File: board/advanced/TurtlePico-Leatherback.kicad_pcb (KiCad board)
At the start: 2 copper layers, 126 parts, among them J1 Micro_SD, J10 AudioJack3, J11 LED, J12 LED, J13 UltraSonic, J14 Debug, J15 Display, J16 TouchDisplay, J17 I/O Pins, J2 Jack-DC, J3 USB_C_Receptacle_USB2.0_16P, J4 RMotor, J5 LMotor, J6 FR_ESC, J7 FL_ESC, J8 RR_ESC, J9 RL_ESC, Q1 DMP6050SSD, Q2 2SC4213, Q3 2SC4213, SW1 SW_Bootsel, SW2 SW_Reset, SW3 SW_{R}, SW4 SW_{L}, SW5 SW_DIP_x04, U1 RP2350B-QFN80, U2 W25Q128JVS, U3 AP63203WU, U4 STUSB4500QTR, U5 DRV8835DSSR, U6 INA260, U7 BNO086, U8 BME280, U9 PCM5102A, Y1 ABM8-272-T3, Y2 ABS06-32.768KHZ-T

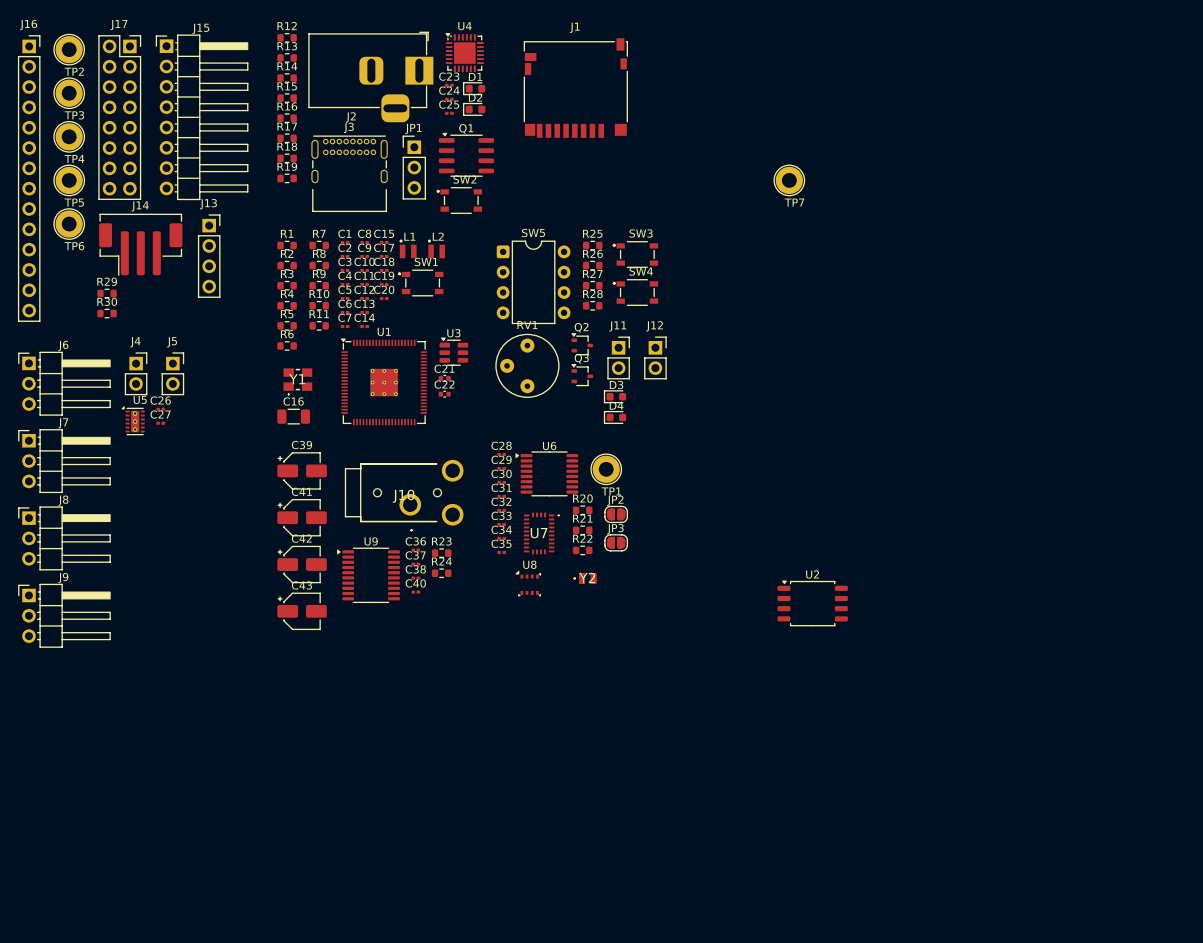
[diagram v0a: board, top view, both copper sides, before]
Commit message: put footprints and change schematics
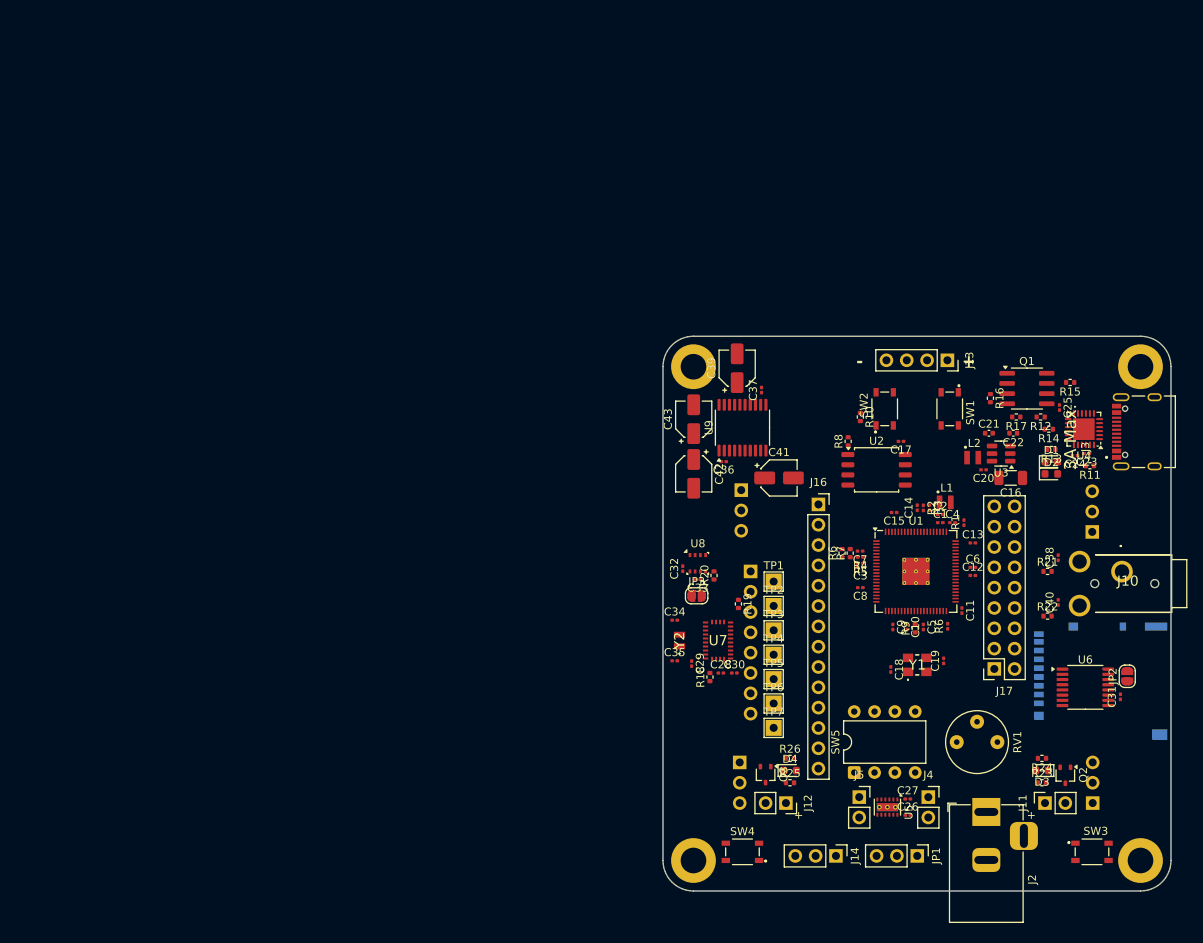
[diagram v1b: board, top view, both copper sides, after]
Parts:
- removed R29: 2k, Resistor_SMD:R_0603_1608Metric
- removed R30: 1k, Resistor_SMD:R_0603_1608Metric
- removed the R7 at (111.6, 66.1)
- removed the R8 at (111.6, 68.6)
- added G***: LOGO, PCBWay:PCBWay, B.Cu at (191.9, 90.8)
- added G***: LOGO, JinPro:JinPro, B.Cu at (178.7, 90.8)
- added R6: 4.7k, Resistor_SMD:R_0402_1005Metric, F.Cu at (176.9, 104.5)
- added REF**: MountingHole_3.2mm_M3_DIN965_Pad, MountingHole:MountingHole_3.2mm_M3_DIN965_Pad, F.Cu at (214.2, 142.9)
- added REF**: MountingHole_3.2mm_M3_DIN965_Pad, MountingHole:MountingHole_3.2mm_M3_DIN965_Pad, F.Cu at (158.3, 81.2)
- added REF**: MountingHole_3.2mm_M3_DIN965_Pad, MountingHole:MountingHole_3.2mm_M3_DIN965_Pad, F.Cu at (214.2, 81.2)
- added REF**: MountingHole_3.2mm_M3_DIN965_Pad, MountingHole:MountingHole_3.2mm_M3_DIN965_Pad, F.Cu at (158.3, 142.9)
- J1: footprint Connector_Card:microSD_HC_Hirose_DM3D-SF -> Connector_Card:microSD_HC_Hirose_DM3AT-SF-PEJM5; moved to B.Cu
- J11: value LED -> LED_{R}
- J12: value LED -> LED_{L}
- J14: footprint Connector_JST:JST_PH_B3B-PH-SM4-TB_1x03-1MP_P2.00mm_Vertical -> Connector_PinHeader_2.54mm:PinHeader_1x03_P2.54mm_Vertical
- J15, J6, J7, J8, J9: moved to B.Cu
- J17: value I/O Pins -> Conn_02x09_Odd_Even; footprint Connector_PinSocket_2.54mm:PinSocket_2x08_P2.54mm_Vertical -> Connector_PinSocket_2.54mm:PinSocket_2x09_P2.54mm_Vertical
- J3: footprint Connector_USB:USB_C_Receptacle_GCT_USB4085 -> NELTRON_5077CR-16SMC2-BK-TR:NELTRON_5077CR-16SMC2-BK-TR
- R1, R2, R3, R4, R5, R6: footprint Resistor_SMD:R_0603_1608Metric -> Resistor_SMD:R_0201_0603Metric
- R10: renamed from R12; footprint Resistor_SMD:R_0603_1608Metric -> Resistor_SMD:R_0402_1005Metric
- R11: renamed from R13; footprint Resistor_SMD:R_0603_1608Metric -> Resistor_SMD:R_0402_1005Metric
- R12: renamed from R14; footprint Resistor_SMD:R_0603_1608Metric -> Resistor_SMD:R_0402_1005Metric
- R13: renamed from R15; footprint Resistor_SMD:R_0603_1608Metric -> Resistor_SMD:R_0402_1005Metric
- R14: renamed from R16; footprint Resistor_SMD:R_0603_1608Metric -> Resistor_SMD:R_0402_1005Metric
- R15: renamed from R17; footprint Resistor_SMD:R_0603_1608Metric -> Resistor_SMD:R_0402_1005Metric
- R16: renamed from R18; footprint Resistor_SMD:R_0603_1608Metric -> Resistor_SMD:R_0402_1005Metric
- R17: renamed from R19; footprint Resistor_SMD:R_0603_1608Metric -> Resistor_SMD:R_0402_1005Metric
- R18: renamed from R20; footprint Resistor_SMD:R_0603_1608Metric -> Resistor_SMD:R_0402_1005Metric
- R19: renamed from R21; footprint Resistor_SMD:R_0603_1608Metric -> Resistor_SMD:R_0402_1005Metric
- R20: renamed from R22; footprint Resistor_SMD:R_0603_1608Metric -> Resistor_SMD:R_0402_1005Metric
- R21: renamed from R23; footprint Resistor_SMD:R_0603_1608Metric -> Resistor_SMD:R_0402_1005Metric
- R22: renamed from R24; footprint Resistor_SMD:R_0603_1608Metric -> Resistor_SMD:R_0402_1005Metric
- R23: renamed from R25; footprint Resistor_SMD:R_0603_1608Metric -> Resistor_SMD:R_0402_1005Metric
- R24: renamed from R26; footprint Resistor_SMD:R_0603_1608Metric -> Resistor_SMD:R_0402_1005Metric
- R25: renamed from R27; footprint Resistor_SMD:R_0603_1608Metric -> Resistor_SMD:R_0402_1005Metric
- R26: renamed from R28; footprint Resistor_SMD:R_0603_1608Metric -> Resistor_SMD:R_0402_1005Metric
- R7: renamed from R9; footprint Resistor_SMD:R_0603_1608Metric -> Resistor_SMD:R_0402_1005Metric
- R8: renamed from R10; footprint Resistor_SMD:R_0603_1608Metric -> Resistor_SMD:R_0402_1005Metric
- R9: renamed from R11; footprint Resistor_SMD:R_0603_1608Metric -> Resistor_SMD:R_0402_1005Metric
- TP1, TP2, TP3, TP4, TP5, TP6, TP7: footprint TestPoint:TestPoint_Loop_D2.50mm_Drill1.85mm -> TestPoint:TestPoint_THTPad_2.0x2.0mm_Drill1.0mm
- moved J8 137.7 mm to (208.2, 135.8)
- moved J6 134.6 mm to (208.2, 101.9)
- moved J17 133.2 mm to (195.9, 119.0), turned to 180 degrees
- moved J2 116.7 mm to (194.9, 136.9), turned to 90 degrees
- moved J14 115.3 mm to (176.1, 142.4), turned to -90 degrees
- moved J16 114.1 mm to (174.0, 98.4)
- moved J4 112.9 mm to (187.7, 135.0)
- moved R11 112.6 mm to (207.9, 93.6), turned to 180 degrees
- moved TP2 112.2 mm to (168.4, 111.1)
- moved TP3 110.7 mm to (168.4, 114.2)
- moved TP4 109.3 mm to (168.4, 117.2)
- moved JP1 108.6 mm to (186.3, 142.4), turned to -90 degrees
- moved TP5 107.9 mm to (168.4, 120.3)
- moved TP6 106.5 mm to (168.4, 123.3)
- moved J3 106.3 mm to (212.3, 89.4), turned to 90 degrees
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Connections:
- net TRIG renamed TRIG/UART_{RX}
- C40 pad 1: Net-(C38-Pad1) -> Net-(C40-Pad1)
- J10 pad R: Net-(C38-Pad1) -> Net-(C40-Pad1)
- J13 pad 3: Net-(J13-Pin_3) -> Echo/UART_{TX}
- J17 pad 10: I/O_{6} -> I/O_{8}
- J17 pad 11: I/O_{7} -> I/O_{9}
- J17 pad 12: I/O_{8} -> I/O_{10}
- J17 pad 13: I/O_{9} -> I/O_{11}
- J17 pad 14: I/O_{10} -> I/O_{12}
- J17 pad 15: I/O_{11} -> I/O_{13}
- J17 pad 16: I/O_{12} -> I/O_{14}
- J17 pad 8: GND -> I/O_{6}
- J17 pad 9: GND -> I/O_{7}
- Q1 pad 7: Net-(Q1A-D1-Pad7) -> VBUS
- Q1 pad 8: Net-(Q1A-D1-Pad7) -> VBUS
- R15 pad 2: Net-(Q1A-D1-Pad7) -> VBUS_{USB}
- R22 pad 2: Net-(C38-Pad1) -> Net-(C40-Pad1)
- U1 pad 40: Net-(U1-GPIO32) -> I/O_{0}
- U1 pad 42: Net-(U1-GPIO33) -> I/O_{1}
- U1 pad 43: I/O_{0} -> I/O_{2}
- U1 pad 44: I/O_{1} -> I/O_{3}
- U1 pad 45: I/O_{2} -> I/O_{4}
- U1 pad 46: I/O_{3} -> I/O_{5}
- U1 pad 47: I/O_{4} -> I/O_{6}
- U1 pad 48: I/O_{5} -> I/O_{7}
- U1 pad 52: I/O_{6} -> I/O_{8}
- U1 pad 53: I/O_{7} -> I/O_{9}
- U1 pad 54: I/O_{8} -> I/O_{10}
- U1 pad 55: I/O_{9} -> I/O_{11}
- U1 pad 56: I/O_{10} -> I/O_{12}
- U1 pad 57: I/O_{11} -> I/O_{13}
- U1 pad 58: I/O_{12} -> I/O_{14}
- U1 pad 77: Echo -> Echo/UART_{TX}
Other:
- board outline added: 63.5 x 69.3 mm
- board text added: "+"
- board text added: "-"
- board text added: "3A Max."
- board text added: "B"
- board text added: "Leatherback"
- board text added: "R"
- board text added: "Turtle Pico v2.0"
- board text added: "Y"

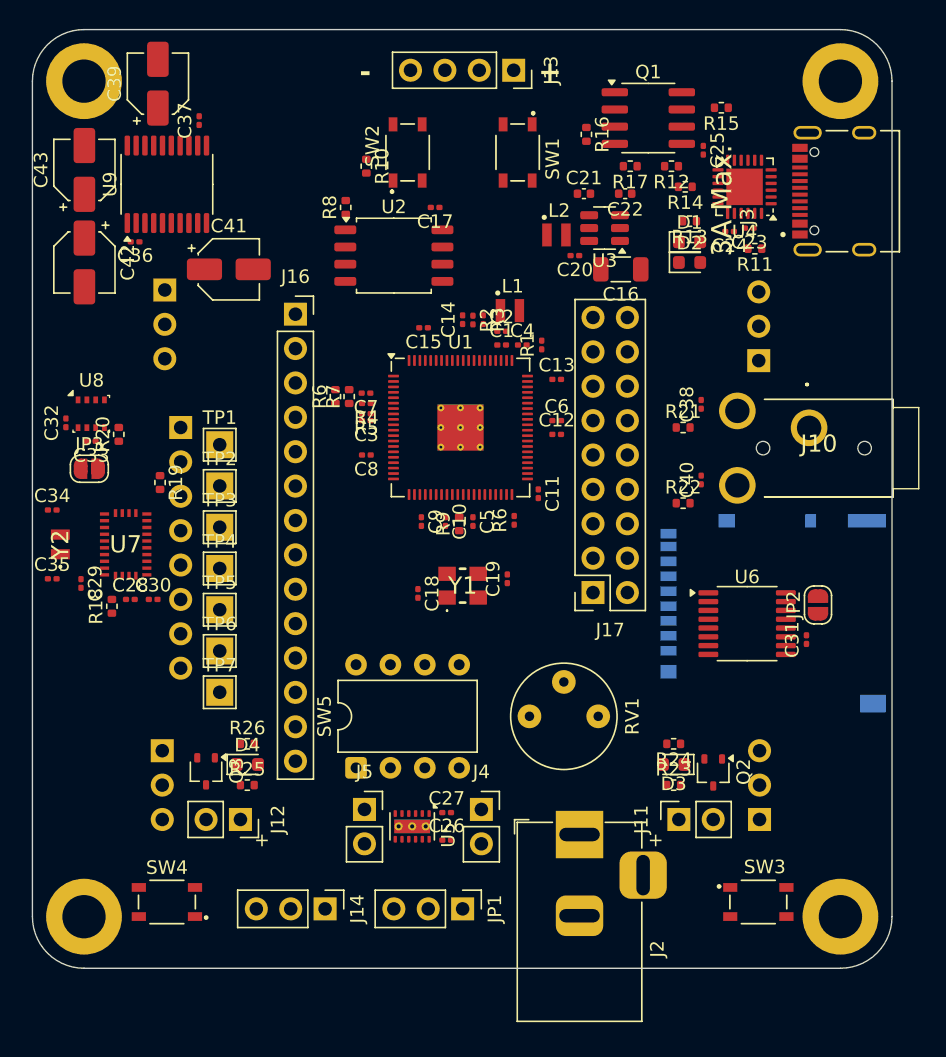
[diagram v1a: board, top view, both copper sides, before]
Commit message: change schematics and complete wiring
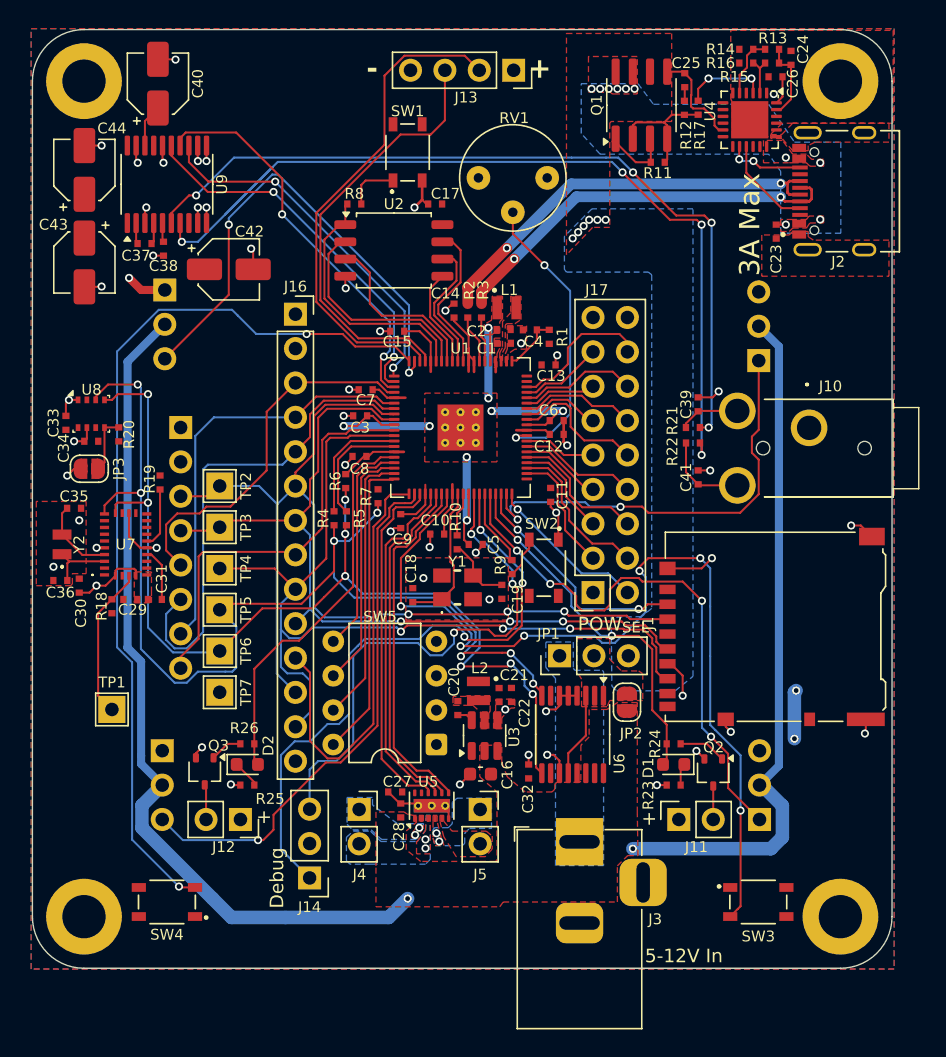
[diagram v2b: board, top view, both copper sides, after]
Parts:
- removed the D1 at (203.1, 93.1)
- removed the D2 at (203.1, 94.6)
- removed the R10 at (179.2, 87.5)
- removed the R11 at (207.9, 93.6)
- removed the R6 at (190.1, 113.7)
- added C26: 0.1u, C_0402_1005Metric_small_pads:C_0402_1005Metric_small_pads, F.Cu at (209.4, 80.9)
- added R16: 10k, C_0402_1005Metric_small_pads:C_0402_1005Metric_small_pads, F.Cu at (207.3, 79.9)
- added R9: 10k, C_0402_1005Metric_small_pads:C_0402_1005Metric_small_pads, F.Cu at (190.0, 117.1)
- C1, C10, C11, C12, C13, C14, C15, C17, C18, C19, C2, C20, C3, C4, C5, C6, C7, C8, C9: footprint Capacitor_SMD:C_0201_0603Metric -> C_0402_1005Metric_small_pads:C_0402_1005Metric_small_pads
- C16: footprint Capacitor_SMD:C_1206_3216Metric -> Capacitor_SMD:C_0603_1608Metric
- C21, C22: footprint Capacitor_SMD:C_0402_1005Metric -> C_0402_1005Metric_small_pads:C_0402_1005Metric_small_pads
- C23: value 1u -> 4.7u; footprint Capacitor_SMD:C_0201_0603Metric -> C_0402_1005Metric_small_pads:C_0402_1005Metric_small_pads
- C24: value 1u -> 0.1u; footprint Capacitor_SMD:C_0201_0603Metric -> C_0402_1005Metric_small_pads:C_0402_1005Metric_small_pads
- C25: value 0.1u -> 1u; footprint Capacitor_SMD:C_0201_0603Metric -> C_0402_1005Metric_small_pads:C_0402_1005Metric_small_pads
- C27: renamed from C26; footprint Capacitor_SMD:C_0201_0603Metric -> C_0402_1005Metric_small_pads:C_0402_1005Metric_small_pads
- C28: renamed from C27; footprint Capacitor_SMD:C_0201_0603Metric -> C_0402_1005Metric_small_pads:C_0402_1005Metric_small_pads
- C29: renamed from C28; footprint Capacitor_SMD:C_0201_0603Metric -> C_0402_1005Metric_small_pads:C_0402_1005Metric_small_pads
- C30: renamed from C29; footprint Capacitor_SMD:C_0201_0603Metric -> C_0402_1005Metric_small_pads:C_0402_1005Metric_small_pads
- C31: renamed from C30; footprint Capacitor_SMD:C_0201_0603Metric -> C_0402_1005Metric_small_pads:C_0402_1005Metric_small_pads
- C32: renamed from C31; footprint Capacitor_SMD:C_0201_0603Metric -> C_0402_1005Metric_small_pads:C_0402_1005Metric_small_pads
- C33: renamed from C32; footprint Capacitor_SMD:C_0201_0603Metric -> C_0402_1005Metric_small_pads:C_0402_1005Metric_small_pads
- C34: renamed from C33; footprint Capacitor_SMD:C_0201_0603Metric -> C_0402_1005Metric_small_pads:C_0402_1005Metric_small_pads
- C35: renamed from C34; footprint Capacitor_SMD:C_0201_0603Metric -> C_0402_1005Metric_small_pads:C_0402_1005Metric_small_pads
- C36: renamed from C35; footprint Capacitor_SMD:C_0201_0603Metric -> C_0402_1005Metric_small_pads:C_0402_1005Metric_small_pads
- C37: renamed from C36; footprint Capacitor_SMD:C_0201_0603Metric -> C_0402_1005Metric_small_pads:C_0402_1005Metric_small_pads
- C38: renamed from C37; footprint Capacitor_SMD:C_0201_0603Metric -> C_0402_1005Metric_small_pads:C_0402_1005Metric_small_pads
- C39: renamed from C38; footprint Capacitor_SMD:C_0201_0603Metric -> C_0402_1005Metric_small_pads:C_0402_1005Metric_small_pads
- C41: renamed from C40; footprint Capacitor_SMD:C_0201_0603Metric -> C_0402_1005Metric_small_pads:C_0402_1005Metric_small_pads
- J1: moved to F.Cu
- R1, R2, R3, R4, R5: footprint Resistor_SMD:R_0201_0603Metric -> C_0402_1005Metric_small_pads:C_0402_1005Metric_small_pads
- R10: renamed from R9; footprint Resistor_SMD:R_0402_1005Metric -> C_0402_1005Metric_small_pads:C_0402_1005Metric_small_pads
- R11: renamed from R16; footprint Resistor_SMD:R_0402_1005Metric -> C_0402_1005Metric_small_pads:C_0402_1005Metric_small_pads
- R12: renamed from R17; footprint Resistor_SMD:R_0402_1005Metric -> C_0402_1005Metric_small_pads:C_0402_1005Metric_small_pads
- R13, R14, R15: value 1k -> 5.1k; footprint Resistor_SMD:R_0402_1005Metric -> C_0402_1005Metric_small_pads:C_0402_1005Metric_small_pads
- R17: renamed from R12; footprint Resistor_SMD:R_0402_1005Metric -> C_0402_1005Metric_small_pads:C_0402_1005Metric_small_pads
- R18, R19, R20, R21, R22, R23, R24, R25, R26, R6, R7, R8: footprint Resistor_SMD:R_0402_1005Metric -> C_0402_1005Metric_small_pads:C_0402_1005Metric_small_pads
- U1: footprint Package_DFN_QFN:QFN-80-1EP_10x10mm_P0.4mm_EP3.4x3.4mm_ThermalVias -> RP2350_80QFN_minimal:RP2350-QFN-80-1EP_10x10_P0.4mm_EP3.4x3.4mm_ThermalVias
- U4: value STUSB4500QTR -> CYPD3177-24LQ; footprint Package_DFN_QFN:QFN-24-1EP_4x4mm_P0.5mm_EP2.7x2.7mm -> Package_DFN_QFN:QFN-24-1EP_4x4mm_P0.5mm_EP2.75x2.75mm
- moved G1 42.9 mm to (213.1, 116.3)
- moved RV1 39.8 mm to (192.6, 88.4), turned to 90 degrees
- moved C16 38.7 mm to (187.6, 132.4)
- moved U3 38.5 mm to (187.9, 129.6), turned to 90 degrees
- moved C22 38.0 mm to (189.9, 126.6), turned to -90 degrees
- moved C21 37.6 mm to (189.0, 126.6), turned to -90 degrees
- moved G2 34.8 mm to (210.6, 120.1)
- moved C20 34.5 mm to (186.0, 127.5), turned to 90 degrees
- moved L2 34.2 mm to (187.5, 126.3), turned to -90 degrees
- moved SW2 32.3 mm to (192.3, 117.2), turned to -90 degrees
- moved C32 22.7 mm to (191.2, 132.2)
- moved TP1 21.1 mm to (160.4, 127.6)
- moved JP1 20.0 mm to (193.5, 123.7), turned to 90 degrees
- moved JP2 15.8 mm to (198.5, 127.1), turned to -90 degrees
- moved U6 15.3 mm to (194.4, 129.5), turned to -90 degrees
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- renumbered C39 to C40, C41 to C42, C42 to C43, C43 to C44, D3 to D1, D4 to D2, G*** to G1, G*** to G2, J3 to J2, J2 to J3, REF** to REF1, REF** to REF2, REF** to REF3, REF** to REF4
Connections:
- C23 pad 1: +2V8 -> VBUS_{USB}
- C24 pad 1: Net-(U4-VREG_1V2) -> VDDD
- C25 pad 1: VBUS_{USB} -> VBUS_{PD}
- J3 pad 1: VBUS_{JACK} -> Net-(JP1-A)
- JP1 pad 1: VBUS_{USB} -> Net-(JP1-A)
- JP1 pad 3: VBUS_{USB} -> VBUS_{PD}
- Q1 pad 5: VBUS_{USB} -> VBUS_{PD}
- Q1 pad 6: VBUS_{USB} -> VBUS_{PD}
- Q1 pad 7: VBUS -> VBUS_{USB}
- Q1 pad 8: VBUS -> VBUS_{USB}
- R13 pad 1: Net-(U4-POWER_OK2) -> Net-(U4-ISNK_COARSE)
- R13 pad 2: Net-(D1-K) (its old number) -> VDDD
- R14 pad 1: Net-(U4-POWER_OK3) -> GND
- R14 pad 2: Net-(D2-K) (its old number) -> Net-(U4-ISNK_COARSE)
- R15 pad 1: Net-(U4-DISCH) -> Net-(U4-VBUS_MAX)
- R15 pad 2: VBUS_{USB} -> VDDD
- R17 pad 1: Net-(U4-VBUS_EN_SNK) -> Net-(U4-VBUS_FET_EN)
- R2 pad 1: D+0 -> D+
- R3 pad 1: D-0 -> D-
- R4 pad 1: Net-(U1-GPIO8) -> Net-(U1-GPIO14)
- R5 pad 1: Net-(U1-GPIO9) -> Net-(U1-GPIO15)
- SW2 pad 1: Net-(R10-Pad2) -> GND
- SW2 pad 2: +2V8 -> Net-(R9-Pad1)
- U1 pad 1: LED_{L} -> I2S_{SCK}
- U1 pad 11: SPI_{MISO} -> Display_{BL}
- U1 pad 12: ESC_{RL} -> SPI_{MISO}
- U1 pad 13: MOTOR_A_{EN} -> Net-(U1-GPIO14)
- U1 pad 14: MOTOR_B_{IN} -> Net-(U1-GPIO15)
- U1 pad 16: ESC_{RR} -> LED_{L}
- U1 pad 17: MOTOR_A_{IN} -> SW_{DIP}4
- U1 pad 18: LED_{R} -> SW_{DIP}3
- U1 pad 19: I2S_{SCK} -> SW_{DIP}2
- U1 pad 2: Display_{RST} -> I2S_{WS}
- U1 pad 20: I2S_{WS} -> SW_{DIP}1
- U1 pad 21: I2S_{SD} -> TOUCH_{CS}
- U1 pad 22: SW_{R} -> ESC_{RL}
- U1 pad 23: SW_{DIP}1 -> MOTOR_A_{IN}
- U1 pad 25: SW_{DIP}2 -> MOTOR_A_{EN}
- U1 pad 26: SW_{DIP}3 -> MOTOR_B_{IN}
- U1 pad 27: SW_{DIP}4 -> MOTOR_B_{EN}
- U1 pad 28: SD_{CS} -> SW_{R}
- U1 pad 3: Display_{DC} -> I2S_{SD}
- U1 pad 35: unconnected-(U1-RUN-Pad35) -> RUN
- U1 pad 36: ESC_{FR} -> ESC_{RR}
- U1 pad 37: MOTOR_B_{EN} -> LED_{R}
- U1 pad 38: Display_{BL} -> SD_{CS}
- U1 pad 39: TOUCH_{CS} -> ESC_{FR}
- U1 pad 6: Net-(U1-GPIO8) -> Display_{RST}
- U1 pad 7: Net-(U1-GPIO9) -> Display_{DC}
- U1 pad 8: SPI_{SCK} -> SPI_{MOSI}
- U1 pad 9: SPI_{MOSI} -> SPI_{SCK}
- U4 pad 1: CC1 -> GND
- U4 pad 10: GND -> unconnected-(U4-FLIP-Pad10)
- U4 pad 11: unconnected-(U4-ATTACH-Pad11) -> VBUS_{PD}
- U4 pad 12: GND -> unconnected-(U4-HPI_SDA-Pad12)
- U4 pad 13: GND -> unconnected-(U4-HPI_SCL-Pad13)
- U4 pad 14: Net-(U4-POWER_OK3) -> CC2
- U4 pad 15: unconnected-(U4-GPIO-Pad15) -> CC1
- U4 pad 16: Net-(U4-VBUS_EN_SNK) -> unconnected-(U4-NC-Pad16)
- U4 pad 18: Net-(U4-VBUS_VS_DISCH) -> VBUS_{USB}
- U4 pad 19: unconnected-(U4-ALERT-Pad19) -> GND
- U4 pad 2: CC1 -> Net-(U4-VBUS_MAX)
- U4 pad 20: Net-(U4-POWER_OK2) -> unconnected-(U4-NC-Pad20)
- U4 pad 21: Net-(U4-VREG_1V2) -> unconnected-(U4-NC-Pad21)
- U4 pad 23: +2V8 -> VDDD
- U4 pad 24: VBUS -> Net-(U4-VCCD)
- U4 pad 3: unconnected-(U4-NC-Pad3) -> Net-(U4-VBUS_FET_EN)
- U4 pad 4: CC2 -> unconnected-(U4-SAFE_PWR_EN-Pad4)
- U4 pad 5: CC2 -> Net-(U4-ISNK_COARSE)
- U4 pad 6: +2V8 -> GND
- U4 pad 7: SCL -> unconnected-(U4-~{HPI_INT}-Pad7)
- U4 pad 8: SDA -> unconnected-(U4-GPIO_1-Pad8)
- U4 pad 9: Net-(U4-DISCH) -> unconnected-(U4-FAULT-Pad9)
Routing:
- net VCC: track 0.00 -> 114.1 mm, vias 0 -> 2
- net SDA: track 0.00 -> 83.2 mm, vias 0 -> 7
- net GND: track 0.00 -> 76.3 mm, vias 0 -> 54
- net SCL: track 0.00 -> 76.2 mm, vias 0 -> 8
- net SPI_{MOSI}: track 0.00 -> 73.0 mm, vias 0 -> 3
- net Net-(U9-OUTR): track 0.00 -> 72.1 mm, vias 0 -> 4
- net SW_{R}: track 0.00 -> 68.6 mm, vias 0 -> 6
- net SPI_{MISO}: track 0.00 -> 68.2 mm, vias 0 -> 3
- net SW_{L}: track 0.00 -> 67.0 mm, vias 0 -> 2
- net Net-(U9-OUTL): track 0.00 -> 60.3 mm, vias 0 -> 4
- net SPI_{SCK}: track 0.00 -> 59.6 mm, vias 0 -> 3
- net SWD: track 0.00 -> 46.4 mm, vias 0 -> 3
- net ESC_{RR}: track 0.00 -> 41.1 mm, vias 0 -> 4
- net ESC_{RL}: track 0.00 -> 39.6 mm, vias 0 -> 1
- net SW_{CLK}: track 0.00 -> 39.4 mm, vias 0 -> 3
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- added copper zone on F.Cu, net +1V1
- added copper zone on F.Cu, net +3.3V
- added copper zone on B.Cu, net GND
- added copper zone on F.Cu, net GND
- added copper zone on B.Cu, net Net-(J4-Pin_1)
- added copper zone on F.Cu, net Net-(J4-Pin_1)
- added copper zone on B.Cu, net Net-(J4-Pin_2)
- added copper zone on F.Cu, net Net-(J4-Pin_2)
- added copper zone on B.Cu, net Net-(J5-Pin_1)
- added copper zone on F.Cu, net Net-(J5-Pin_1)
- added copper zone on F.Cu, net Net-(J5-Pin_2)
- added copper zone on B.Cu, net Net-(JP1-A)
- added copper zone on F.Cu, net Net-(U1-VREG_LX)
- added copper zone on F.Cu, net Net-(U3-SW)
- added copper zone on F.Cu, net VBUS
- added copper zone on B.Cu, net VBUS_{PD}
- added copper zone on F.Cu, net VBUS_{PD}
- added copper zone on B.Cu, net VBUS_{USB}
- added copper zone on F.Cu, net VBUS_{USB}
- added copper zone on F.Cu, net VCC
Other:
- rule pad_to_mask_clearance: 0 -> 0.03
- board text added: "3A Max"
- board text added: "5-12V In"
- board text added: "POW_{SEL}"
- board text removed: "3A Max."
